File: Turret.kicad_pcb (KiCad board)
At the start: 2 copper layers, 58.4 x 129.5 mm, 20 parts, among them J1 Conn_01x04_Pin, J12 Conn_01x02_Pin, J13 Conn_01x02_Pin, J14 Conn_01x02_Pin, J15 Conn_01x02_Pin, J16 Conn_01x02_Pin, J17 Conn_01x02_Pin, J18 Conn_01x02_Pin, J19 Conn_01x02_Pin, J2 Conn_01x02_Pin, J20 Conn_01x02_Pin, J21 Conn_01x02_Pin, J3 Conn_01x02_Pin, J4 Conn_01x02_Pin, J5 Conn_01x02_Pin, J6 Conn_01x02_Pin, J7 Conn_01x02_Pin, J8 Conn_01x02_Pin, J9 Conn_01x02_Pin

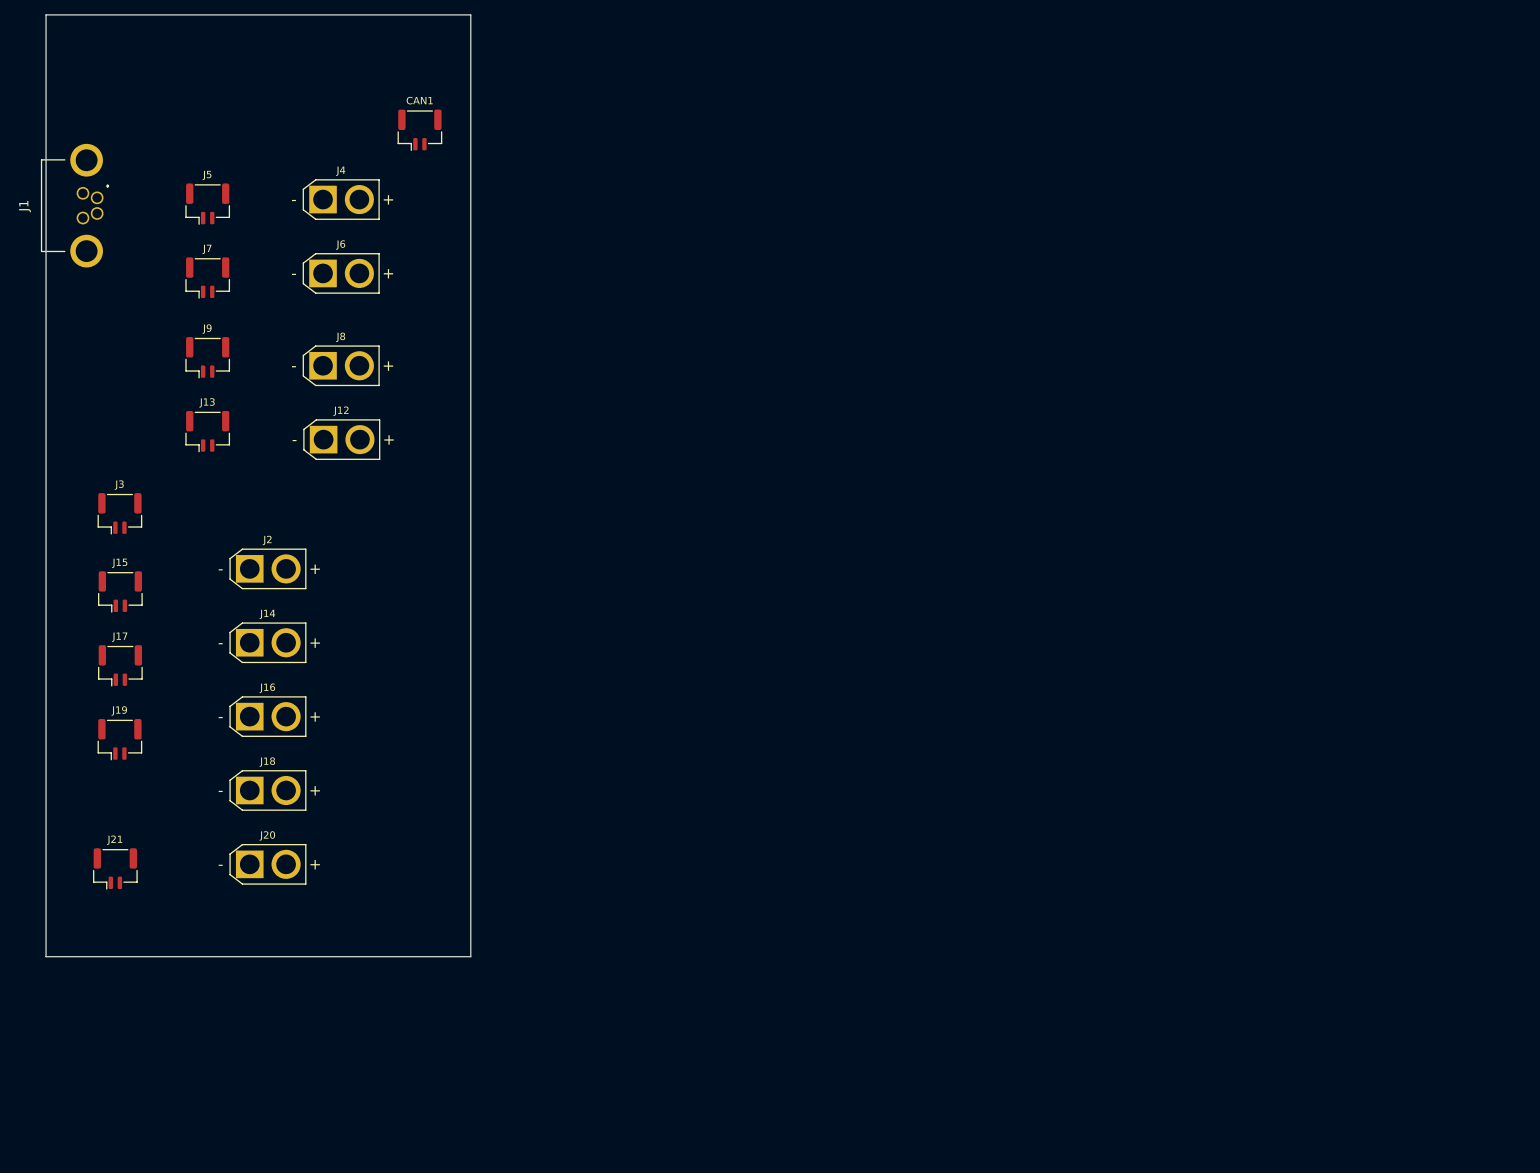
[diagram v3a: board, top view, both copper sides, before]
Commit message: turret dimensions
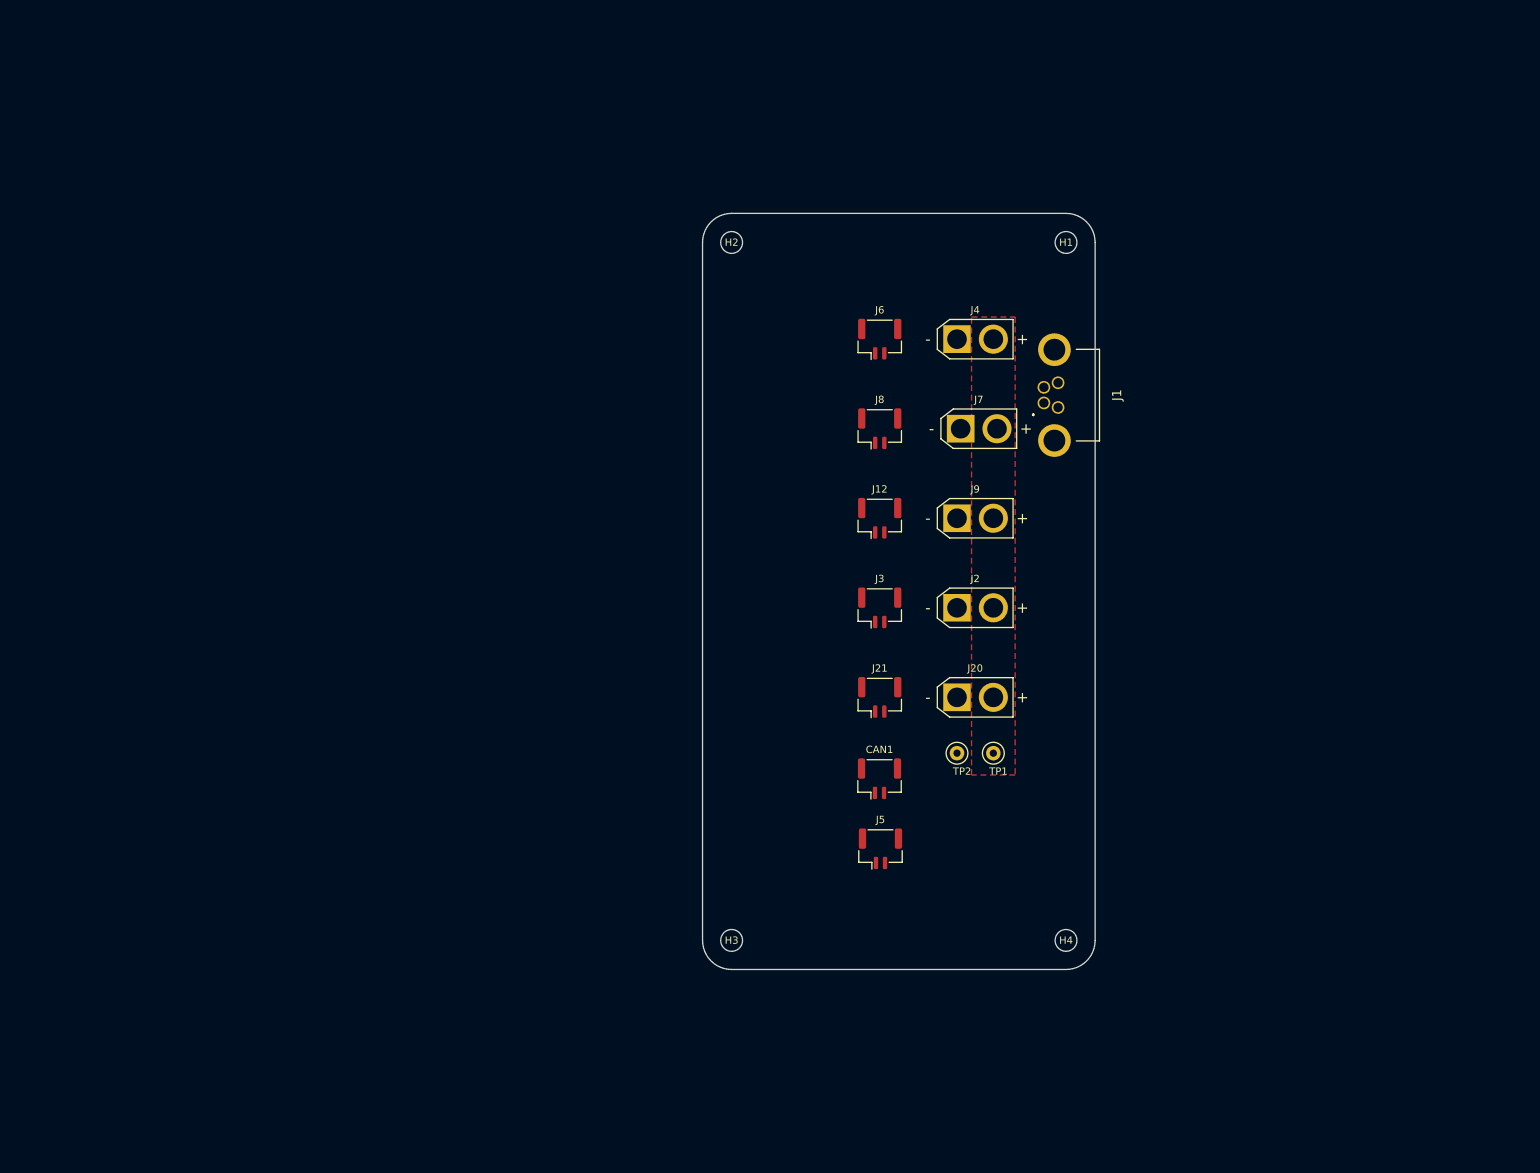
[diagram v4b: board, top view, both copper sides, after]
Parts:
- removed J13, J15, J17, J19: Conn_01x02_Pin, Connector_JST:JST_GH_BM02B-GHS-TBT_1x02-1MP_P1.25mm_Vertical
- removed J14, J16, J18: Conn_01x02_Pin, Connector_AMASS:AMASS_XT30U-F_1x02_P5.0mm_Vertical
- added H1: MountingHole, MountingHole:MountingHole_3mm, F.Cu at (153.0, 44.0)
- added H2: MountingHole, MountingHole:MountingHole_3mm, F.Cu at (107.0, 44.0)
- added H3: MountingHole, MountingHole:MountingHole_3mm, F.Cu at (107.0, 140.0)
- added H4: MountingHole, MountingHole:MountingHole_3mm, F.Cu at (153.0, 140.0)
- added TP1: TestPoint, TestPoint:TestPoint_Loop_D1.80mm_Drill1.0mm_Beaded, F.Cu at (143.0, 114.2)
- added TP2: TestPoint, TestPoint:TestPoint_Loop_D1.80mm_Drill1.0mm_Beaded, F.Cu at (138.0, 114.2)
- J12, J6, J8: footprint Connector_AMASS:AMASS_XT30U-F_1x02_P5.0mm_Vertical -> Connector_JST:JST_GH_BM02B-GHS-TBT_1x02-1MP_P1.25mm_Vertical
- J7, J9: footprint Connector_JST:JST_GH_BM02B-GHS-TBT_1x02-1MP_P1.25mm_Vertical -> Connector_AMASS:AMASS_XT30U-F_1x02_P5.0mm_Vertical
- moved J1 137.3 mm to (151.9, 66.7), turned to 90 degrees
- moved J5 128.2 mm to (127.5, 127.4)
- moved CAN1 109.4 mm to (127.3, 117.8)
- moved J21 107.7 mm to (127.4, 106.6)
- moved J7 105.6 mm to (138.5, 69.6)
- moved J9 105.4 mm to (138.0, 81.9)
- moved J3 105.3 mm to (127.4, 94.3)
- moved J20 100.0 mm to (138.0, 106.6)
- moved J2 97.4 mm to (138.0, 94.3)
- moved J4 89.3 mm to (138.0, 57.3)
- moved J12 77.3 mm to (127.4, 81.9)
- moved J6 77.1 mm to (127.4, 57.3)
- moved J8 77.1 mm to (127.4, 69.6)
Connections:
- J12 pad 1: Net-(J12-Pin_1) -> /Shooter_CANL
- J12 pad 2: Net-(J12-Pin_2) -> /Shooter_CANH
- J2 pad 1: GND1 -> GND
- J2 pad 2: /Shooter_Vin -> +24V
- J20 pad 1: GND2 -> GND
- J20 pad 2: /Turret_Vin -> +24V
- J4 pad 1: Net-(J4-Pin_1) -> GND
- J4 pad 2: Net-(J4-Pin_2) -> +24V
- J6 pad 1: Net-(J6-Pin_1) -> /Shooter_CANL
- J6 pad 2: Net-(J6-Pin_2) -> /Shooter_CANH
- J7 pad 1: Net-(J7-Pin_1) -> GND
- J7 pad 2: Net-(J7-Pin_2) -> +24V
- J8 pad 1: Net-(J8-Pin_1) -> /Shooter_CANL
- J8 pad 2: Net-(J8-Pin_2) -> /Shooter_CANH
- J9 pad 1: Net-(J9-Pin_1) -> GND
- J9 pad 2: Net-(J9-Pin_2) -> +24V
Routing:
- added copper zone on F.Cu, net +24V
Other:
- board size 58.4 x 129.5 mm -> 54 x 104 mm

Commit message: Add trace
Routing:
- net /Shooter_CANL: track 0.00 -> 37.0 mm
- net /Shooter_CANH: track 0.00 -> 37.0 mm
- added copper zone on F.Cu, net GND
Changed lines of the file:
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@@
     (style (thickness 0.15) (arrow_length 1.27) (text_position_mode 0) (extension_height 0.58642) (extension_offset 0.5) keep_text_aligned)
   )
+  (segment (start 126.75 59.25) (end 126.75 96.2025) (width 0.25) (layer "F.Cu") (net 13))
+  (segment (start 128 59.25) (end 128 96.2025) (width 0.25) (layer "F.Cu") (net 14))
   (zone (net 4) (net_name "+24V") (layer "F.Cu") (hatch edge 0.5)
     (priority 1)
@@
       )
     )
+  )
+  (zone (net 3) (net_name "GND") (layer "F.Cu") (hatch edge 0.5)
+    (priority 1)
+    (connect_pads (clearance 0.5))
+    (min_thickness 0.25) (filled_areas_thickness no)
+    (fill yes (thermal_gap 0.5) (thermal_bridge_width 0.5))
+    (polygon
+      (pts
+        (xy 140 54.25)
+        (xy 140 117.25)
+        (xy 135.636 117.221)
+        (xy 135.89 54.102)
+      )
+    )

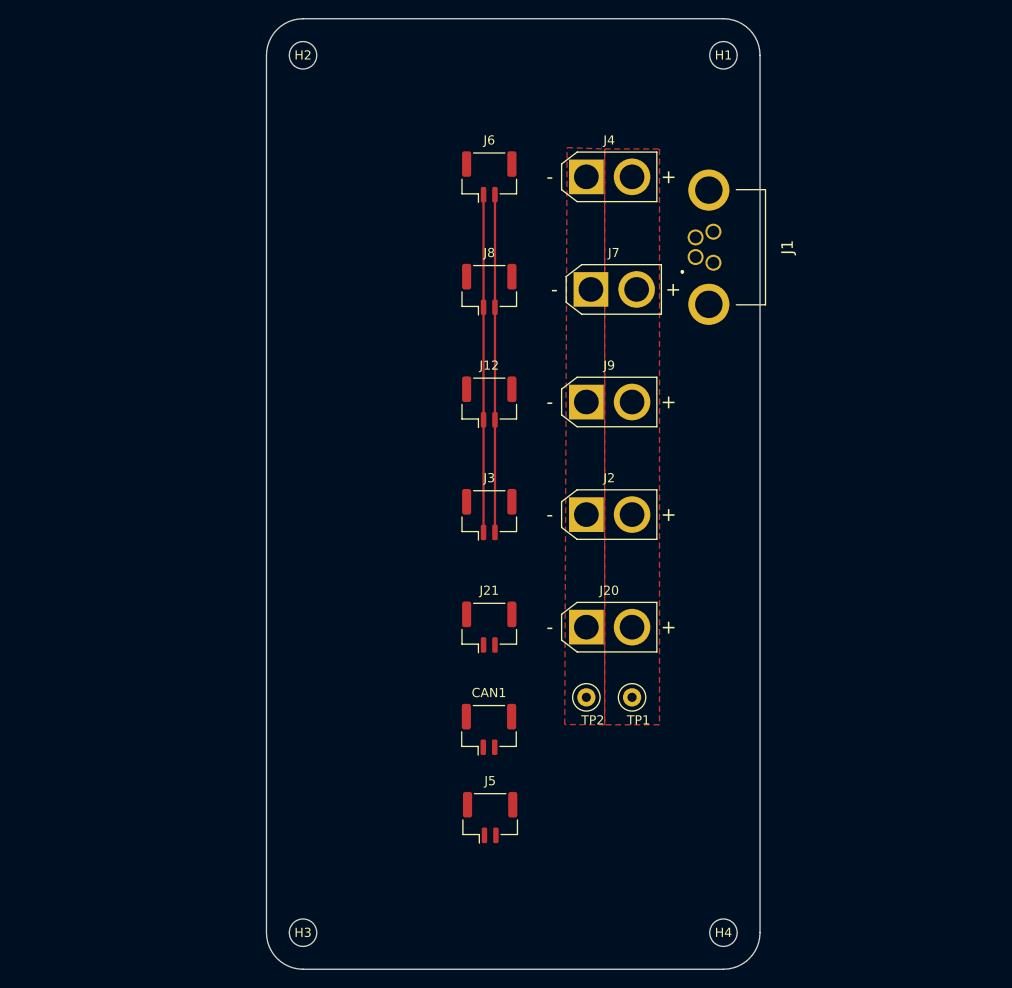
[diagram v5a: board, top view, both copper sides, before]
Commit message: Fix CAN and change schematic
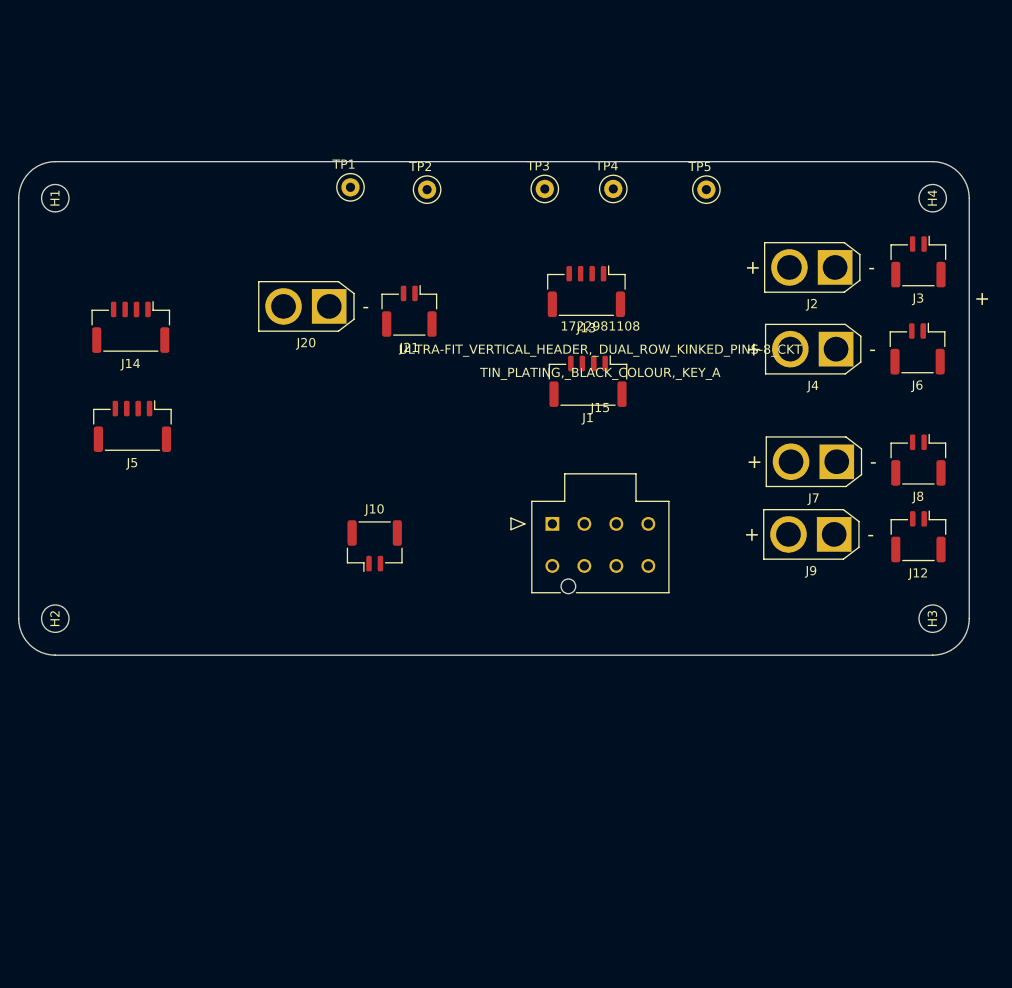
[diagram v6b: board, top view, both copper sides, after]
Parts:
- removed CAN1: Conn_01x02_Pin, Connector_JST:JST_GH_BM02B-GHS-TBT_1x02-1MP_P1.25mm_Vertical
- added J10: Conn_01x02_Pin, Connector_JST:JST_GH_BM02B-GHS-TBT_1x02-1MP_P1.25mm_Vertical, F.Cu at (114.8, 97.7)
- added J13: Conn_01x04_Pin, Connector_JST:JST_GH_BM04B-GHS-TBT_1x04-1MP_P1.25mm_Vertical, F.Cu at (138.0, 69.8)
- added J14: Conn_01x04_Pin, Connector_JST:JST_GH_BM04B-GHS-TBT_1x04-1MP_P1.25mm_Vertical, F.Cu at (88.2, 73.8)
- added J15: Conn_01x08_Pin, ICs:CON_1722981108_MOL, F.Cu at (134.3, 95.3)
- added TP3: TestPoint, TestPoint:TestPoint_Loop_D1.80mm_Drill1.0mm_Beaded, F.Cu at (133.5, 58.6)
- added TP4: TestPoint, TestPoint:TestPoint_Loop_D1.80mm_Drill1.0mm_Beaded, F.Cu at (140.9, 58.6)
- added TP5: TestPoint, TestPoint:TestPoint_Loop_D1.80mm_Drill1.0mm_Beaded, F.Cu at (151.1, 58.7)
- J1: footprint Robomasters:866319112100004 -> Connector_JST:JST_GH_BM04B-GHS-TBT_1x04-1MP_P1.25mm_Vertical
- J5: value Conn_01x02_Pin -> Conn_01x04_Pin; footprint Connector_JST:JST_GH_BM02B-GHS-TBT_1x02-1MP_P1.25mm_Vertical -> Connector_JST:JST_GH_BM04B-GHS-TBT_1x04-1MP_P1.25mm_Vertical
- moved H4 83.6 mm to (175.9, 59.6), turned to 90 degrees
- moved H3 77.0 mm to (175.9, 105.6), turned to 90 degrees
- moved H1 74.8 mm to (79.9, 59.6), turned to 90 degrees
- moved H2 67.3 mm to (79.9, 105.6), turned to 90 degrees
- moved TP1 63.7 mm to (112.2, 58.4), turned to 180 degrees
- moved TP2 58.2 mm to (120.6, 58.7), turned to 180 degrees
- moved J5 58.0 mm to (88.3, 84.6), turned to 180 degrees
- moved J3 54.5 mm to (174.3, 66.6), turned to 180 degrees
- moved J8 50.5 mm to (174.3, 88.3), turned to 180 degrees
- moved J6 50.5 mm to (174.2, 76.1), turned to 180 degrees
- moved J12 49.2 mm to (174.3, 96.7), turned to 180 degrees
- moved J20 45.0 mm to (109.9, 71.5), turned to 180 degrees
- moved J2 38.4 mm to (165.2, 67.2), turned to 180 degrees
- moved J21 35.7 mm to (118.6, 72.0), turned to 180 degrees
- moved J4 33.2 mm to (165.3, 76.2), turned to 180 degrees
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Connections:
- J1 pad 1: Net-(J1-Pin_1) -> GND
- J1 pad 2: Net-(J1-Pin_2) -> /UART_TX
- J1 pad 3: Net-(J1-Pin_3) -> /UART_RX
- J1 pad 4: Net-(J1-Pin_4) -> +3.3V
- J12 pad 1: /Shooter_CANL -> /CANL
- J12 pad 2: /Shooter_CANH -> /CANH
- J2 pad 2: +24V -> /+24V Shooter
- J20 pad 2: +24V -> /+24V Gimbal
- J21 pad 1: /Turret_CANL -> /CANL
- J21 pad 2: /Turret_CANH -> /CANH
- J3 pad 1: /Shooter_CANL -> /CANL
- J3 pad 2: /Shooter_CANH -> /CANH
- J4 pad 2: +24V -> /+24V Shooter
- J5 pad 1: Net-(J5-Pin_1) -> GND
- J5 pad 2: Net-(J5-Pin_2) -> /SWDIO
- J6 pad 1: /Shooter_CANL -> /CANL
- J6 pad 2: /Shooter_CANH -> /CANH
- J7 pad 2: +24V -> /+24V Shooter
- J8 pad 1: /Shooter_CANL -> /CANL
- J8 pad 2: /Shooter_CANH -> /CANH
- J9 pad 2: +24V -> /+24V Shooter
- TP1 pad 1: +24V -> /+24V_Shooter
- TP2 pad 1: GND -> /+24V_Gimbal
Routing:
- net /Shooter_CANL: track 37.0 -> 0.00 mm
- net /Shooter_CANH: track 37.0 -> 0.00 mm
- removed copper zone on F.Cu, net +24V
- removed copper zone on F.Cu, net GND
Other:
- board size 54 x 104 mm -> 104 x 54 mm
